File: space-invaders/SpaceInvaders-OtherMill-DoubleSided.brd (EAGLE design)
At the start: 127 x 101.6 mm, 26 parts, among them J2-J4 TM4C123GXL, J3-J1 TM4C123GXL, J5 Nokia_5110, J6 Nokia_5110, J7 9V, U1 LM7805CT

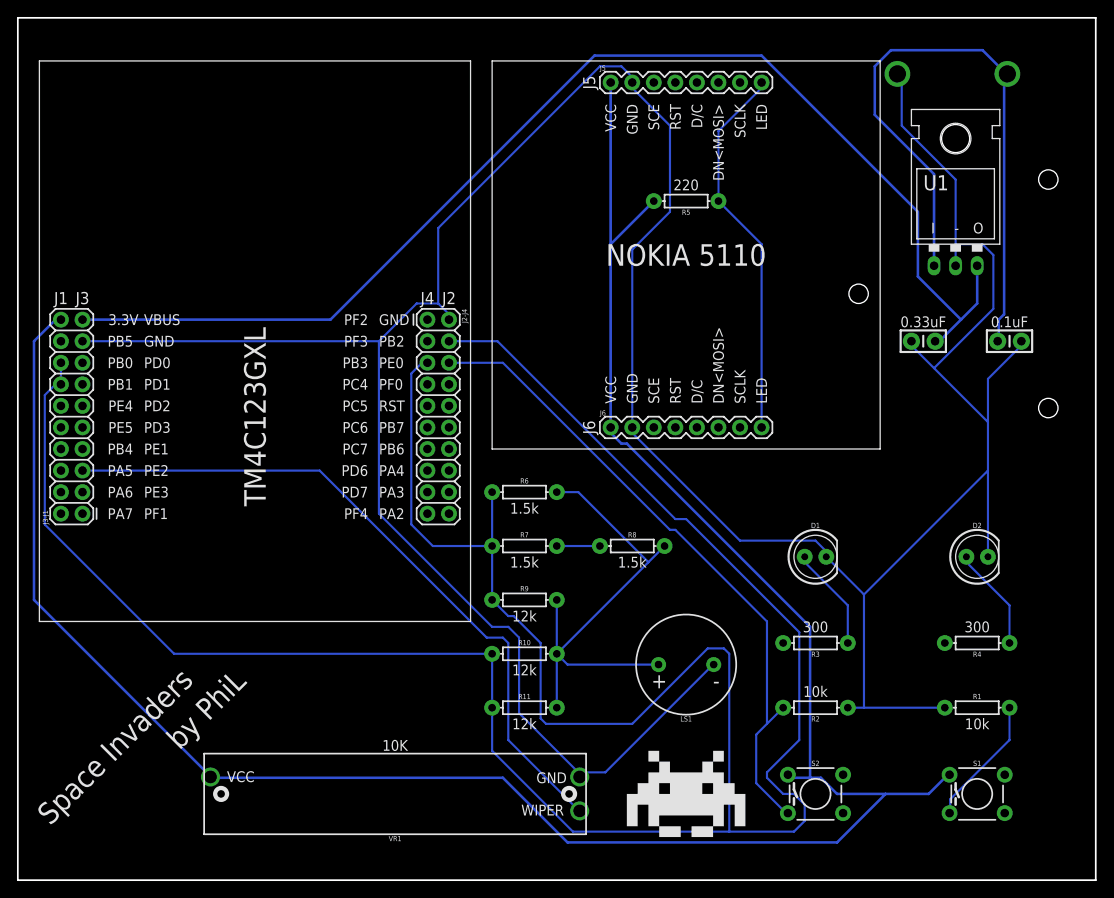
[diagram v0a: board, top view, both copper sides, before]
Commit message: Create OtherMill-compatible SpaceInvaders
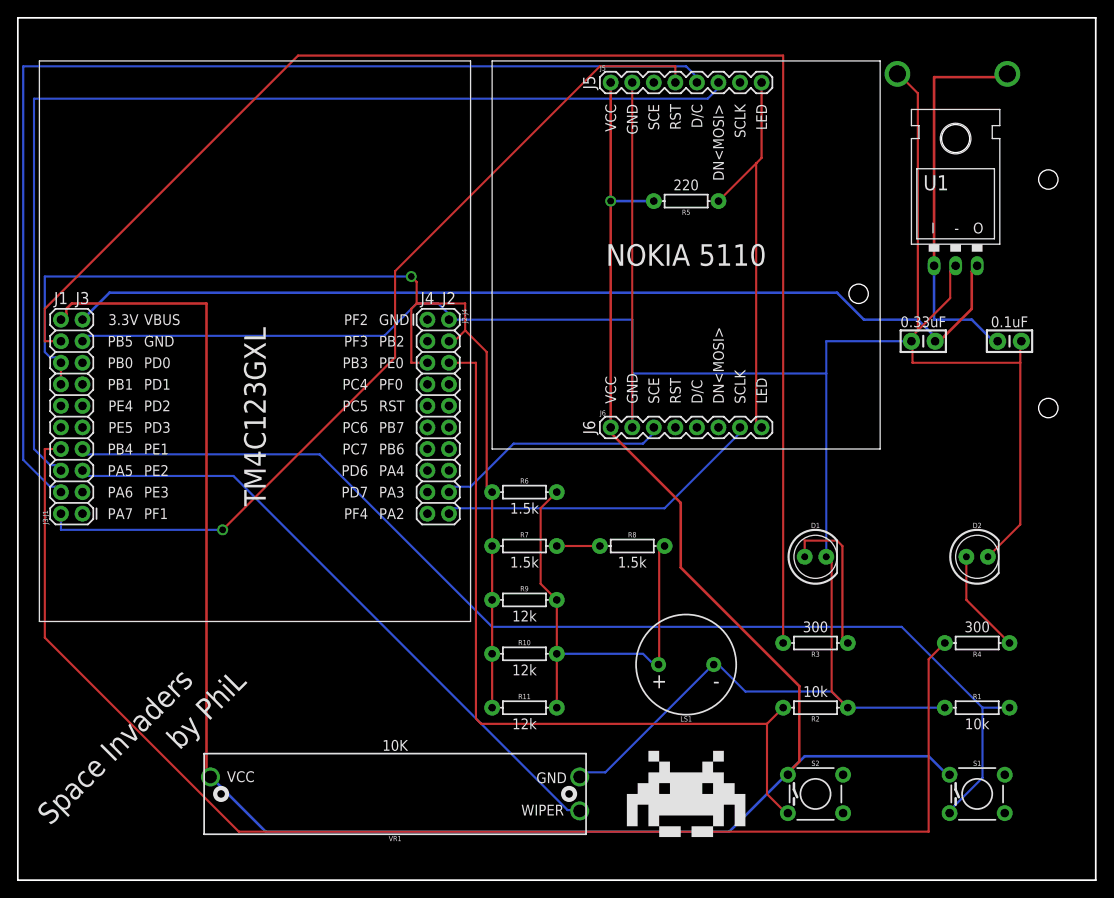
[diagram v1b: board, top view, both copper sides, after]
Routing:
- net PB2: track 321.4 -> 126.7 mm, vias 0 -> 1
- net PB5: track 0.00 -> 174.3 mm
- net PB4: track 0.00 -> 160.8 mm
- net PA6: track 0.00 -> 132.9 mm
- net PA5: track 0.00 -> 127.3 mm
- net PE1: track 15.3 -> 135.9 mm
- net PA7: track 0.00 -> 104.8 mm, vias 0 -> 1
- net GND: track 384.2 -> 333.6 mm
- net PA2: track 0.00 -> 38.9 mm
- net 9V: track 76.0 -> 45.9 mm
- net VBUS: track 145.0 -> 116.4 mm
- net PA3: track 0.00 -> 27.7 mm
- net PE0: track 77.5 -> 93.9 mm
- net PE2: track 81.9 -> 75.2 mm
- net LLED: track 12.3 -> 18.3 mm
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
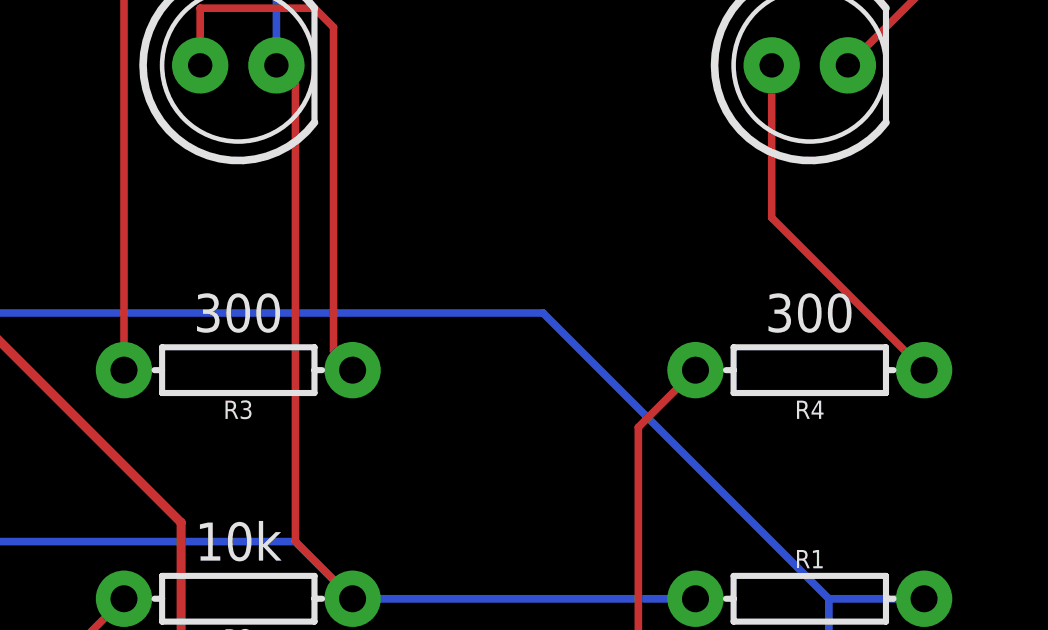
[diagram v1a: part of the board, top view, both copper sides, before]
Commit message: Change LLED and RLED resistor value from 300 to 220
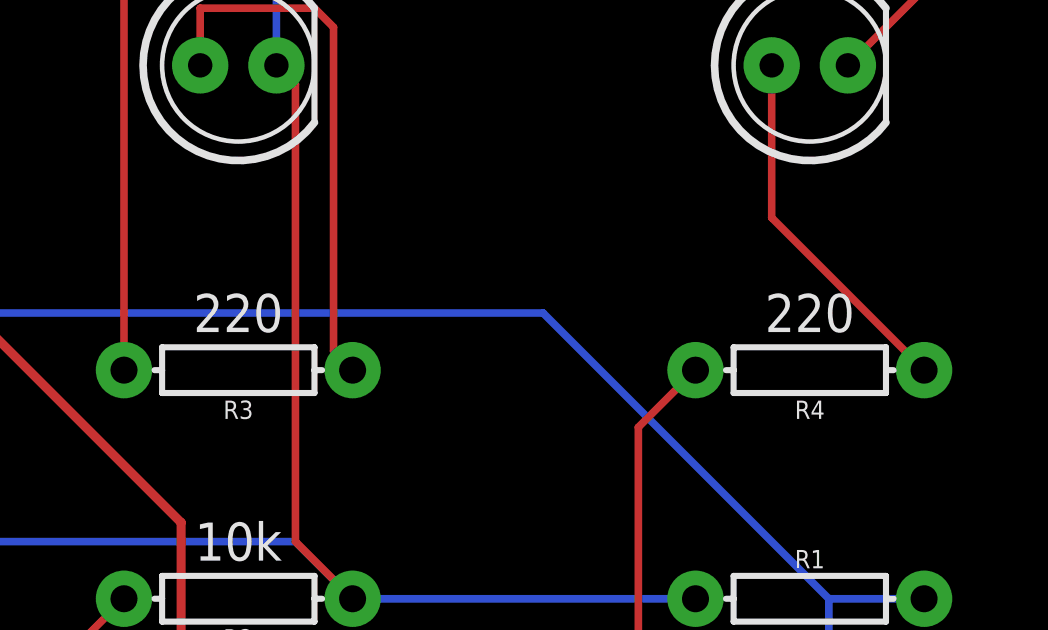
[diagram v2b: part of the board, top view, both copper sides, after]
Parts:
- D1: value YELLOW -> RED
- D2: value RED -> YELLOW
- R3, R4: value 300 -> 220
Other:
- board text removed: "300"
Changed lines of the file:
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@@
 <text x="110.617" y="76.835" size="1.27" layer="21" font="vector" ratio="10" align="center">-</text>
 <text x="78.74" y="82.55" size="1.27" layer="21" font="vector" align="top-center">220</text>
-<text x="93.98" y="30.48" size="1.27" layer="21" font="vector" align="top-center">300</text>
-<text x="113.03" y="30.48" size="1.27" layer="21" font="vector" align="top-center">300</text>
+<text x="93.98" y="30.48" size="1.27" layer="21" font="vector" align="top-center">220</text>
+<text x="113.03" y="30.48" size="1.27" layer="21" font="vector" align="top-center">220</text>
 <text x="93.98" y="21.59" size="1.27" layer="21" font="vector" rot="R180" align="top-center">10k</text>
 <text x="113.03" y="17.78" size="1.27" layer="21" font="vector" rot="R180" align="top-center">10k</text>
@@
 <param name="TopRouterVariant" value="1"/>
 <param name="tpViaShape" value="round"/>
-<param name="PrefDir.1" value="a"/>
+<param name="PrefDir.1" value="*"/>
 <param name="PrefDir.2" value="0"/>
 <param name="PrefDir.3" value="0"/>
@@
 <param name="PrefDir.14" value="0"/>
 <param name="PrefDir.15" value="0"/>
-<param name="PrefDir.16" value="a"/>
+<param name="PrefDir.16" value="-"/>
 <param name="cfVia" value="8"/>
 <param name="cfNonPref" value="5"/>
@@
 <attribute name="PROD_ID" value="CAP-08370" x="116.84" y="63.5" size="1.778" layer="27" display="off"/>
 </element>
-<element name="D1" library="SparkFun-LED" package="LED_5MM" value="YELLOW" x="93.98" y="38.1"/>
-<element name="D2" library="SparkFun-LED" package="LED_5MM" value="RED" x="113.03" y="38.1"/>
+<element name="D1" library="SparkFun-LED" package="LED_5MM" value="RED" x="93.98" y="38.1"/>
+<element name="D2" library="SparkFun-LED" package="LED_5MM" value="YELLOW" x="113.03" y="38.1"/>
 <element name="FRAME1" library="SparkFun-Aesthetics" package="CREATIVE_COMMONS" value="FRAME-LETTER" x="30.48" y="-8.89"/>
 <element name="J2-J4" library="SparkFun-Connectors" package="2X10" value="TM4C123GXL" x="48.26" y="66.04" rot="R270"/>
@@
 <attribute name="PROD_ID" value="RES-09435" x="93.98" y="20.32" size="1.778" layer="27" rot="R180" display="off"/>
 </element>
-<element name="R3" library="SparkFun-Resistors" package="AXIAL-0.3" value="300" x="93.98" y="27.94" rot="R180">
+<element name="R3" library="SparkFun-Resistors" package="AXIAL-0.3" value="220" x="93.98" y="27.94" rot="R180">
 <attribute name="PROD_ID" value="RES-08380" x="93.98" y="27.94" size="1.778" layer="27" rot="R180" display="off"/>
 </element>
-<element name="R4" library="SparkFun-Resistors" package="AXIAL-0.3" value="300" x="113.03" y="27.94" rot="R180">
+<element name="R4" library="SparkFun-Resistors" package="AXIAL-0.3" value="220" x="113.03" y="27.94" rot="R180">
 <attribute name="PROD_ID" value="RES-08380" x="113.03" y="27.94" size="1.778" layer="27" rot="R180" display="off"/>
 </element>

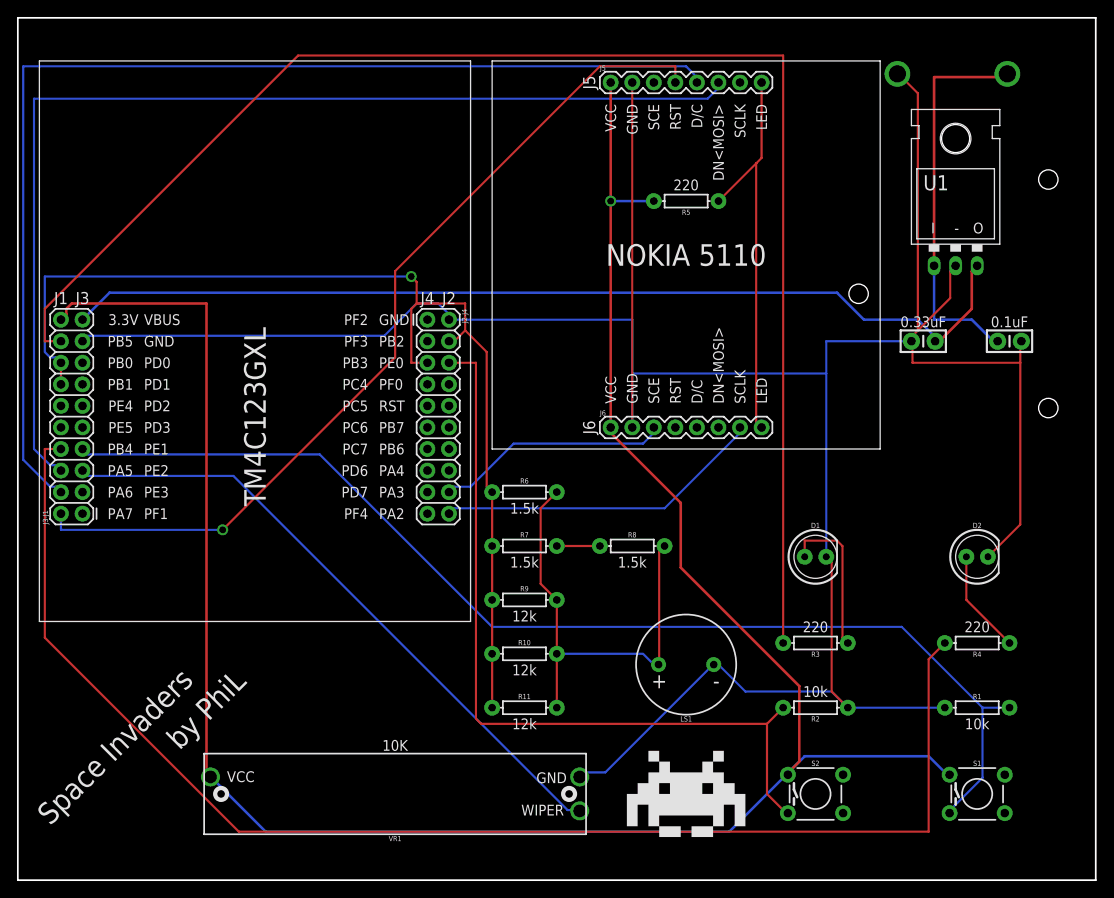
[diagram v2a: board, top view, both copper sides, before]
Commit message: Rip off Autorouter. Will route by hand.
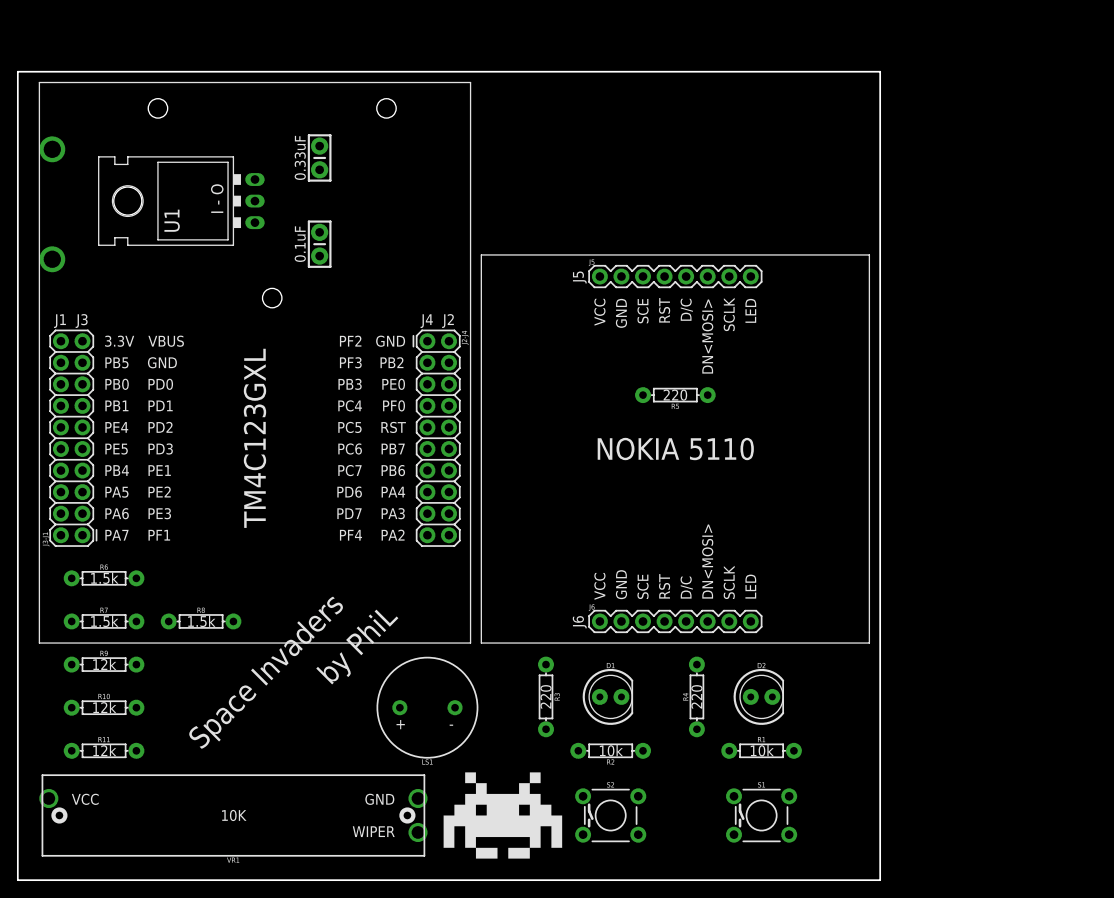
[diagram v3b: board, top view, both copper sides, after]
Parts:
- moved U1 86.4 mm to (24.1, 80.0), turned to 90 degrees
- moved C2 82.1 mm to (35.6, 74.9), turned to 90 degrees
- moved C1 74.3 mm to (35.6, 85.1), turned to 90 degrees
- moved R8 51.6 mm to (21.6, 30.5)
- moved R6 50.6 mm to (10.2, 35.6)
- moved R7 50.3 mm to (10.2, 30.5)
- moved R9 50.1 mm to (10.2, 25.4)
- moved R10 49.9 mm to (10.2, 20.3)
- moved R11 49.8 mm to (10.2, 15.2)
- moved J7 44.4 mm to (57.1, 64.8), turned to 0 degrees
- moved R4 33.6 mm to (80.0, 21.6), turned to 90 degrees
- moved R3 32.4 mm to (62.2, 21.6), turned to 270 degrees
- moved LS1 30.9 mm to (48.3, 20.3)
- moved D2 30.3 mm to (87.6, 21.6)
- moved D1 29.2 mm to (69.8, 21.6)
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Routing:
- net GND: track 333.6 -> 0.00 mm
- net 3.3V: track 265.0 -> 0.00 mm, vias 1 -> 0
- net PB5: track 174.3 -> 0.00 mm
- net PB4: track 160.8 -> 0.00 mm
- net PE1: track 135.9 -> 0.00 mm
- net PA6: track 132.9 -> 0.00 mm
- net PA5: track 127.3 -> 0.00 mm
- net PB2: track 126.7 -> 0.00 mm, vias 1 -> 0
- net VBUS: track 116.4 -> 0.00 mm
- net PA7: track 104.8 -> 0.00 mm, vias 1 -> 0
- net PE0: track 93.9 -> 0.00 mm
- net PE2: track 75.2 -> 0.00 mm
- net DAC_OUT: track 53.8 -> 0.00 mm
- net LED: track 47.5 -> 0.00 mm
- net 9V: track 45.9 -> 0.00 mm
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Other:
- board size 127 x 101.6 mm -> 101.6 x 95.2 mm
- board text added: "I - O"
- board text removed: "I"
- board text removed: "O"
